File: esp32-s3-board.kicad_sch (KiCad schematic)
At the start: 5 parts, among them P1 USB_C_Plug_USB2.0, U1 ESP32-S3, U2 AMS1117-3.3

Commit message: Added journal
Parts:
- removed C2: 10uF, symbol Device:C_Polarized
- removed P1: USB_C_Plug_USB2.0, symbol Connector:USB_C_Plug_USB2.0
- added C2: 10uF, symbol Device:C
- added C3: C, symbol Device:C
- added C4, C5: 15pF, symbol Device:C
- added J1: USB_C_Receptacle_USB2.0_14P, symbol Connector:USB_C_Receptacle_USB2.0_14P
- added R1: 10k, symbol Device:R
- added R2, R3: 5.1k, symbol Device:R
- added R4, R5: 23, symbol Device:R
- added R6: 1k, symbol Device:R
- added U3: W25Q128JVS, Package_SO:SOIC-8_5.3x5.3mm_P1.27mm, symbol Memory_Flash:W25Q128JVS
- added Y1: 40MHz, symbol Device:Crystal_GND24
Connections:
- net +3V3: now also C2.1, R1.1
- net +5V: now also J1.A4 (VBUS), J1.A9 (VBUS), J1.B4 (VBUS), J1.B9 (VBUS)
- net D+: now also J1.A6 (D+), J1.B6 (D+), R5.1; no longer U1.26 (GPIO20/USB_D+)
- net D-: now also J1.A7 (D-), J1.B7 (D-), R4.1; no longer U1.25 (GPIO19/USB_D-)
- net GND: now also C2.2, C3.2, C4.1, C5.1, J1.A1 (GND), J1.A12 (GND), J1.B1 (GND), J1.B12 (GND), J1.S1 (SHIELD), R2.2, R3.2, Y1.2 (G), Y1.4 (G)
- net at U1.4 (CHIP_PU): now also C3.1, R1.2
- net XOUT: now reaches U1.53 (XTAL_N)
- net XOUT: now also R6.2
- net XIN: now reaches U1.54 (XTAL_P)
- net XIN: now also C5.2, Y1.3
- new net: R4.2, U1.25 (GPIO19/USB_D-)
- new net: R5.2, U1.26 (GPIO20/USB_D+)
- new net: C4.2, R6.1, Y1.1
- new net: J1.A5 (CC1), R2.1
- new net: J1.B5 (CC2), R3.1

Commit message: Editted journal
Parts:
- added C6, C7: C, symbol Device:C
- added J2: OV2640, symbol Connector_Generic:Conn_01x24
- added U4: ESP-PSRAM64H, Package_SO:SOIC-8_3.9x4.9mm_P1.27mm, symbol Memory_RAM:ESP-PSRAM32
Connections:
- net +3V3: now also U3.8 (VCC), C6.1, C7.1, U4.8 (VCC)
- net GND: now also U3.4 (GND), C6.2, C7.2, U4.4 (VSS)
- net SPICS1: now reaches U1.28 (SPICS1)
- net SPICS1: now also U4.1 (~{CE})
- net MEMID3: now reaches U1.30 (SPIHD)
- net MEMID3: now also U3.7 (~{HOLD}/~{RESET}/IO_{3}), U4.7 (SIO3)
- net MEMID2: now reaches U1.31 (SPIWP)
- net MEMID2: now also U3.3 (~{WP}/IO_{2}), U4.3 (SIO2)
- net SPICS0: now reaches U1.32 (SPICS0)
- net SPICS0: now also U3.1 (~{CS})
- net MEMID1: now reaches U1.34 (SPIQ)
- net MEMID1: now also U3.2 (DO/IO_{1}), U4.5 (SI/SIO)
- net MEMID0: now reaches U1.35 (SPID)
- net MEMID0: now also U3.5 (DI/IO_{0}), U4.2 (SO/SIO)
- net MEMSCLK: now reaches U1.37 (SPICLK_P)
- net MEMSCLK: now also U3.6 (CLK), U4.6 (SCLK)

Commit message: Added journal
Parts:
- added C10, C11, C8, C9: 10uF, symbol Device:C
- added C12, C13, C15: 4.7uF, symbol Device:C
- added C14, C16: 0.1uF, symbol Device:C
- added R7: R, symbol Device:R
- added R8, R9: 10k, symbol Device:R
- added SW1: SW_Push, symbol Switch:SW_Push
- added U5: NCP1117-2.85_SOT223, Package_TO_SOT_SMD:SOT-223-3_TabPin2, symbol Regulator_Linear:NCP1117-2.85_SOT223
- added U6: NCP1117-1.5_SOT223, Package_TO_SOT_SMD:SOT-223-3_TabPin2, symbol Regulator_Linear:NCP1117-1.5_SOT223
- C1: value 1uF -> 10uF
- C6, C7: value C -> 0.1uF
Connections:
- net +3V3: now also C8.1, C9.1, R7.1, U5.3 (VI), U6.3 (VI)
- net GND: now also J2.15 (Pin_15), J2.2 (Pin_2), U1.52 (GPIO46), C10.2, C11.2, C12.2, C13.2, C14.2, C15.2, C16.2, C8.2, C9.2, R9.2, SW1.1, U5.1 (GND), U6.1 (GND)
- net IO5: now reaches U1.10 (GPIO5)
- net IO5: now also J2.5 (Pin_5)
- net IO6: now reaches U1.11 (GPIO6)
- net IO6: now also J2.7 (Pin_7)
- net IO7: now reaches U1.12 (GPIO7)
- net IO7: now also J2.9 (Pin_9)
- net IO8: now reaches U1.13 (GPIO8)
- net IO8: now also J2.22 (Pin_22)
- net IO9: now reaches U1.14 (GPIO9)
- net IO9: now also J2.21 (Pin_21)
- net IO10: now reaches U1.15 (GPIO10)
- net IO10: now also J2.20 (Pin_20)
- net IO11: now reaches U1.16 (GPIO11)
- net IO11: now also J2.19 (Pin_19)
- net IO12: now reaches U1.17 (GPIO12)
- net IO12: now also J2.18 (Pin_18)
- net IO13: now reaches U1.18 (GPIO13)
- net IO13: now also J2.17 (Pin_17)
- net IO15: now reaches U1.21 (XTAL_32K_P)
- net IO15: now also J2.13 (Pin_13)
- net IO16: now reaches U1.22 (XTAL_32K_N)
- net IO16: now also J2.12 (Pin_12)
- net IO17: now reaches U1.23 (GPIO17)
- net IO17: now also J2.14 (Pin_14)
- net IO18: now reaches U1.24 (GPIO18)
- net IO18: now also J2.16 (Pin_16)
- net at U1.5 (GPIO0): now also R7.2, SW1.2
- net IO4: now reaches U1.9 (GPIO4)
- net IO4: now also J2.3 (Pin_3)
- net +1V5: now reaches J2.10 (Pin_10)
- net +1V5: now also C10.1, C15.1, C16.1, U6.2 (VO)
- net +2V8: now reaches J2.11 (Pin_11)
- net +2V8: now also J2.4 (Pin_4), C11.1, C12.1, C13.1, C14.1, R8.1, U5.2 (VO)
- net at J2.6 (Pin_6): now also R8.2
- net at J2.8 (Pin_8): now also R9.1
- no-connect marks 0 -> 4
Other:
- note added: "Camera"
- note added: "Camera pwoer supply"
- note added: "Crystal occilator"
- note added: "Flash memory"
- note added: "Main power supply"
- note added: "PSRAM"
- note added: "USB"
- moved on the sheet: C1, C2, C3, J2, R1, R4, R5, U1, U2

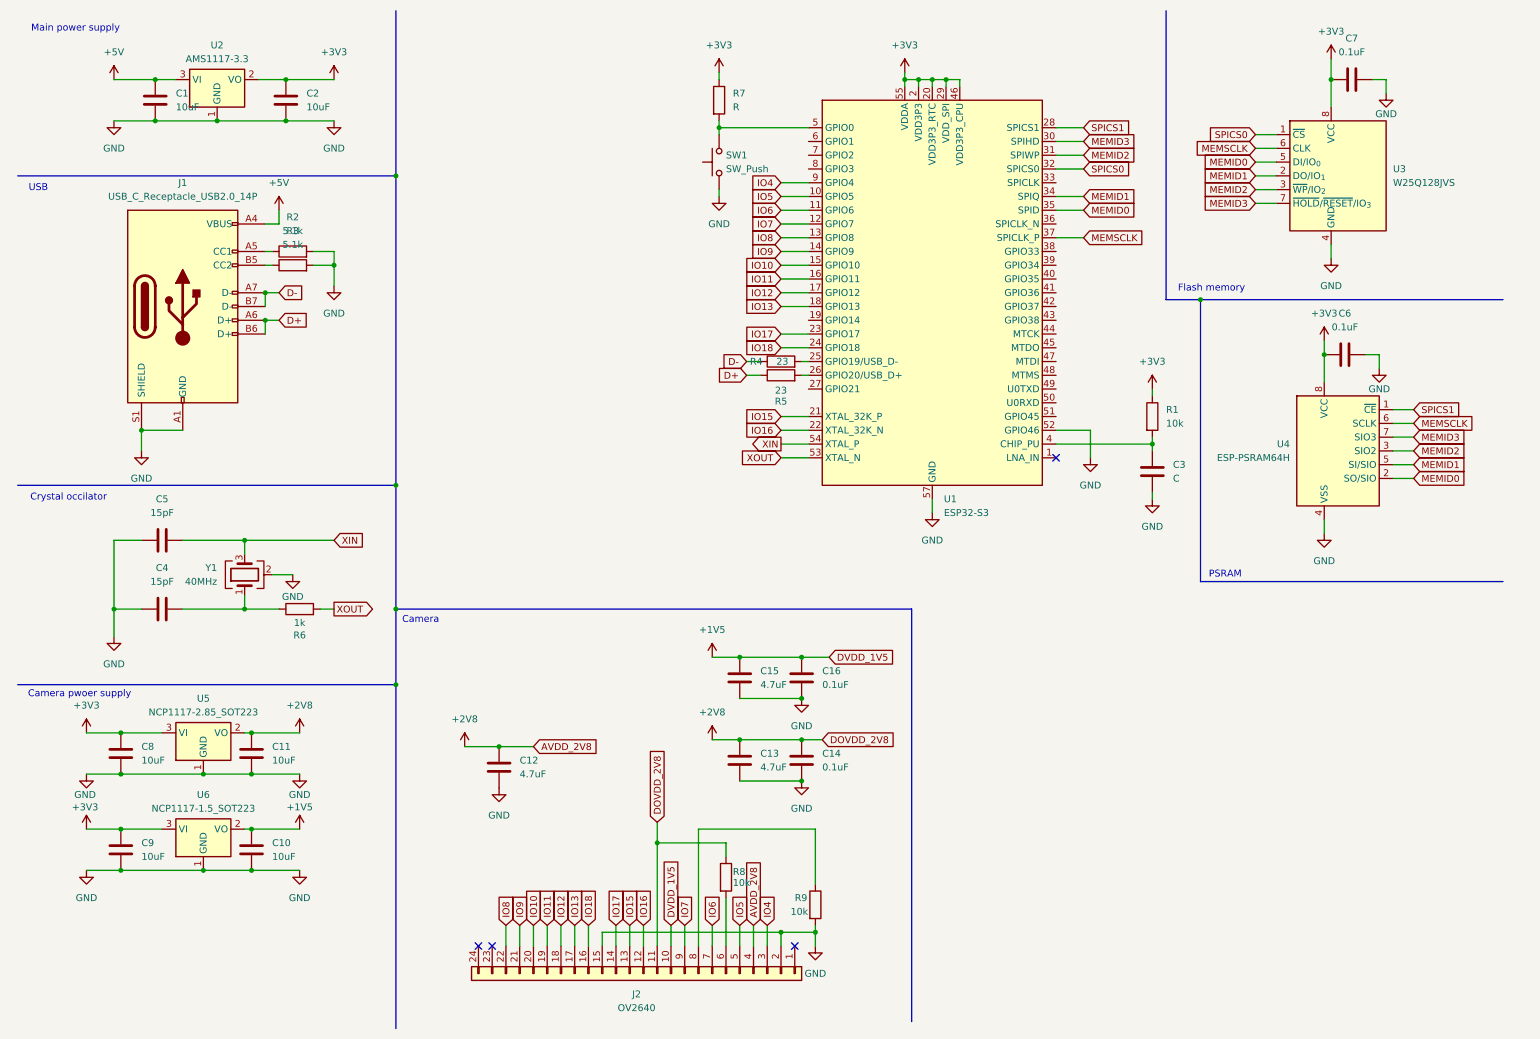
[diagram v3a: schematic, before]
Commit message: Finished writing schematic
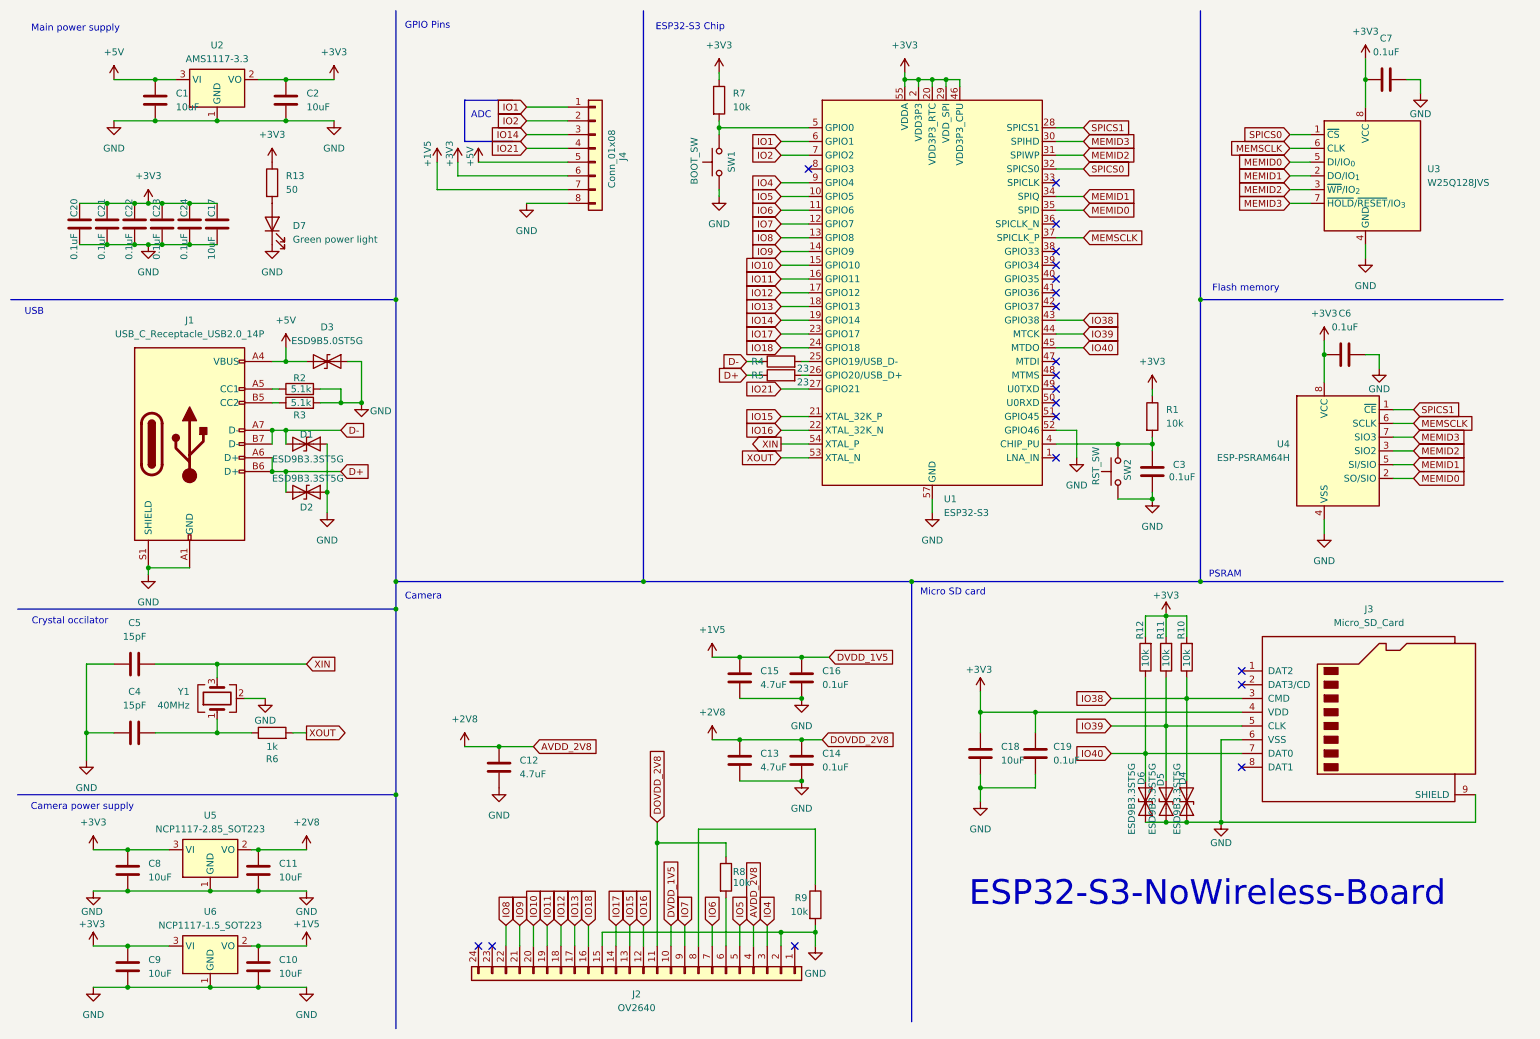
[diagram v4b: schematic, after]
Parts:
- added C17, C18: 10uF, symbol Device:C
- added C19, C20, C21, C22, C23, C24: 0.1uF, symbol Device:C
- added D1, D2, D4, D5, D6: ESD9B3.3ST5G, Diode_SMD:D_SOD-923, symbol Diode:ESD9B3.3ST5G
- added D3: ESD9B5.0ST5G, Diode_SMD:D_SOD-923, symbol Diode:ESD9B5.0ST5G
- added D7: Green power light, symbol Device:LED
- added J3: Micro_SD_Card, symbol Connector:Micro_SD_Card
- added J4: Conn_01x08, symbol Connector_Generic:Conn_01x08
- added R10, R11, R12: 10k, symbol Device:R
- added R13: 50, symbol Device:R
- added SW2: RST_SW, symbol Switch:SW_Push
- C3: value C -> 0.1uF
- R7: value R -> 10k
- SW1: value SW_Push -> BOOT_SW
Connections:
- net +1V5: now also J4.7 (Pin_7)
- net +3V3: now also C17.1, C18.1, C19.1, C20.1, C21.1, C22.1, C23.1, C24.1, J3.4 (VDD), J4.6 (Pin_6), R10.2, R11.2, R12.2, R13.1
- net +5V: now also D3.1 (A1), J4.5 (Pin_5)
- net D+: now also D2.1 (A1)
- net D-: now also D1.1 (A1)
- net GND: now also C17.2, C18.2, C19.2, C20.2, C21.2, C22.2, C23.2, C24.2, D1.2 (A2), D2.2 (A2), D3.2 (A2), D4.1 (A1), D5.1 (A1), D6.1 (A1), D7.1 (K), J3.6 (VSS), J3.9 (SHIELD), J4.8 (Pin_8), SW2.1
- net IO14: now reaches U1.19 (GPIO14)
- net IO14: now also J4.3 (Pin_3)
- net IO21: now reaches U1.27 (GPIO21)
- net IO21: now also J4.4 (Pin_4)
- net at C3.1, R1.2, U1.4 (CHIP_PU): now also SW2.2
- net IO38: now reaches U1.43 (GPIO38)
- net IO38: now also D4.2 (A2), J3.3 (CMD), R10.1
- net IO39: now reaches U1.44 (MTCK)
- net IO39: now also D5.2 (A2), J3.5 (CLK), R11.1
- net IO40: now reaches U1.45 (MTDO)
- net IO40: now also D6.2 (A2), J3.7 (DAT0), R12.1
- net IO1: now reaches U1.6 (GPIO1)
- net IO1: now also J4.1 (Pin_1)
- net IO2: now reaches U1.7 (GPIO2)
- net IO2: now also J4.2 (Pin_2)
- new net: D7.2 (A), R13.2
- no-connect marks 4 -> 20
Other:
- note added: "ADC"
- note added: "Camera power supply"
- note added: "ESP32-S3 Chip"
- note added: "ESP32-S3-NoWireless-Board"
- note added: "GPIO Pins"
- note added: "Micro SD card"
- note removed: "Camera pwoer supply"
- moved on the sheet: C10, C11, C4, C5, C7, C8, C9, J1, R2, R3, R6, U3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

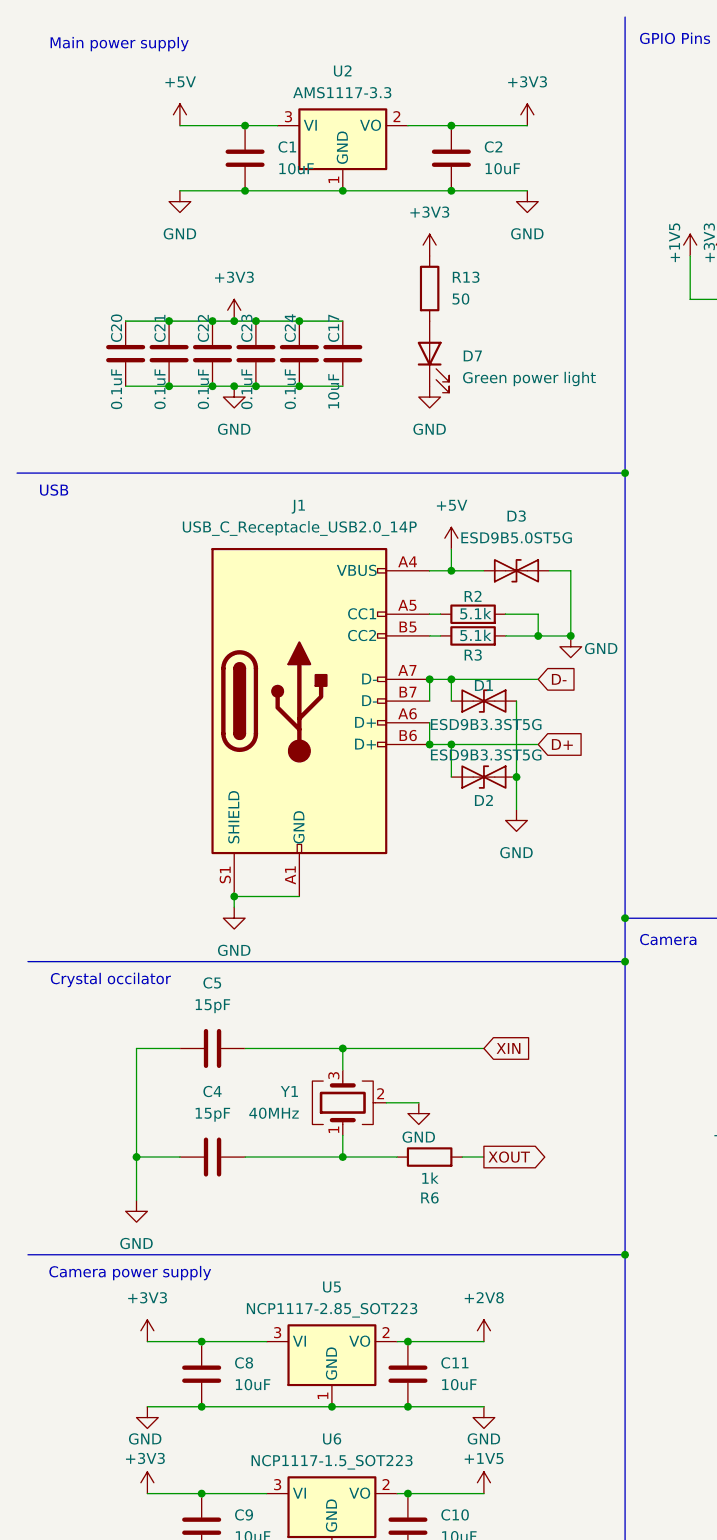
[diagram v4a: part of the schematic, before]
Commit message: Assigned footprint
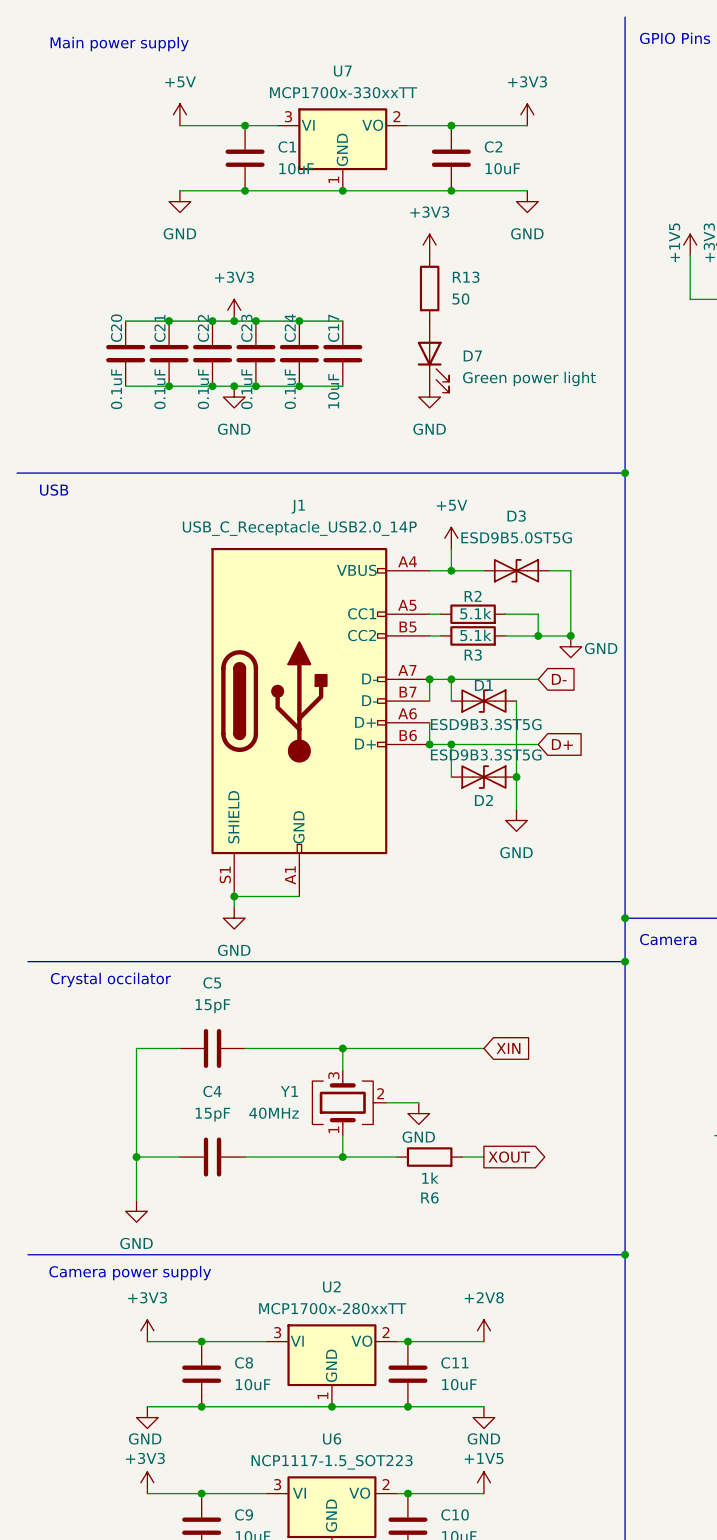
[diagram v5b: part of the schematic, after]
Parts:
- removed U2: AMS1117-3.3, Package_TO_SOT_SMD:SOT-223-3_TabPin2, symbol Regulator_Linear:AMS1117-3.3
- removed U5: NCP1117-2.85_SOT223, Package_TO_SOT_SMD:SOT-223-3_TabPin2, symbol Regulator_Linear:NCP1117-2.85_SOT223
- added U2: MCP1700x-280xxTT, Package_TO_SOT_SMD:SOT-23, symbol Regulator_Linear:MCP1700x-280xxTT
- added U7: MCP1700x-330xxTT, Package_TO_SOT_SMD:SOT-23, symbol Regulator_Linear:MCP1700x-330xxTT
- C1, C10, C11, C12, C13, C14, C15, C16, C17, C18, C19, C2, C20, C21, C22, C23, C24, C3, C4, C5, C6, C7, C8, C9: footprint (none) -> Capacitor_SMD:C_0603_1608Metric_Pad1.08x0.95mm_HandSolder
- D7: footprint (none) -> LED_SMD:LED_0805_2012Metric_Pad1.15x1.40mm_HandSolder
- J1: footprint (none) -> Connector_USB:USB_C_Receptacle_HRO_TYPE-C-31-M-12
- J2: footprint (none) -> Connector_FFC-FPC:Amphenol_F32Q-1A7x1-11024_1x24-1MP_P0.5mm_Horizontal
- J3: footprint (none) -> Connector_Card:microSD_HC_Molex_104031-0811
- J4: footprint (none) -> Connector_PinHeader_2.54mm:PinHeader_1x08_P2.54mm_Horizontal
- R1, R10, R11, R12, R13, R2, R3, R4, R5, R6, R7, R8, R9: footprint (none) -> Resistor_SMD:R_0603_1608Metric_Pad0.98x0.95mm_HandSolder
- SW1, SW2: footprint (none) -> Button_Switch_SMD:SW_Push_SPST_NO_Alps_SKRK
- Y1: footprint (none) -> Crystal:Crystal_SMD_3225-4Pin_3.2x2.5mm_HandSoldering
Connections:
- net +2V8: now also U2.2 (VO)
- net +3V3: now also U2.3 (VI), U7.2 (VO)
- net +5V: now also U7.3 (VI)
- net GND: now also U2.1 (GND), U7.1 (GND)
